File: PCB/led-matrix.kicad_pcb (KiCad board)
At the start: 2 copper layers, 58 x 18 mm, 25 parts, among them J1 Conn_02x03_Odd_Even

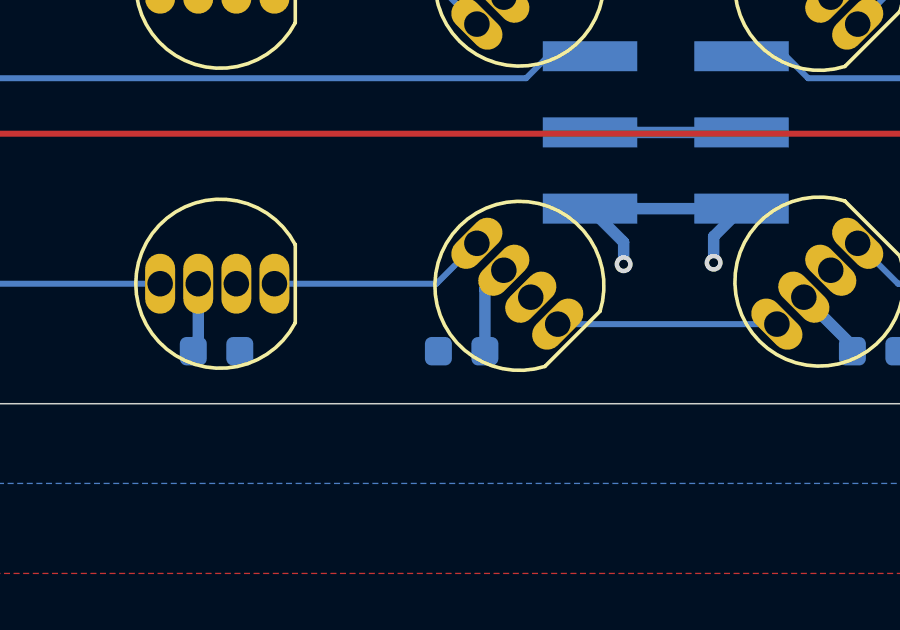
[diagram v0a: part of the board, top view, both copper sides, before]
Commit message: Resolve ground plane island issue
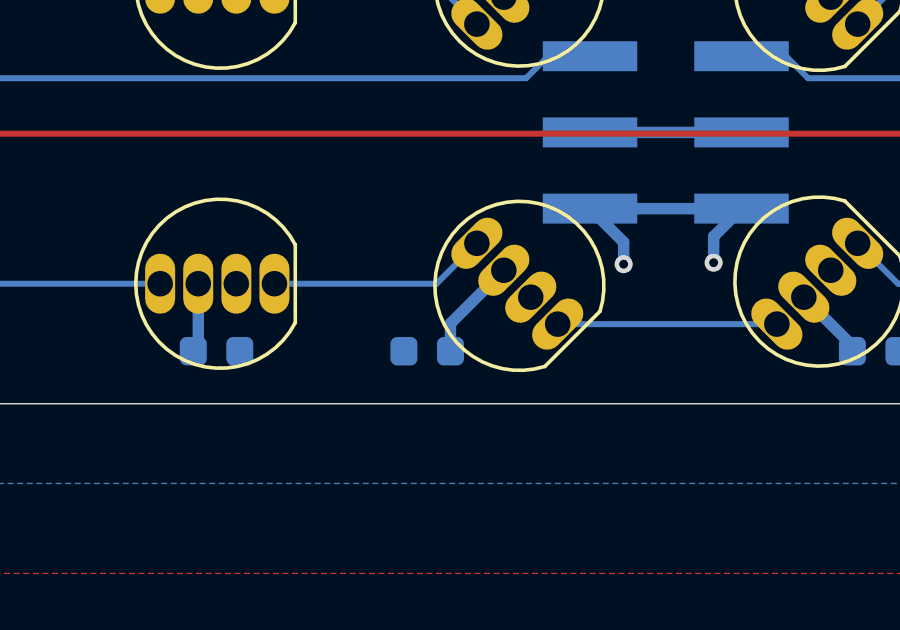
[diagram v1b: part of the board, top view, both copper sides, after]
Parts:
- moved C9 1.15 mm to (95.4, 70.8)
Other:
- board text added: "ImSeanConroy/LED-Matrix (v0.3)"
- board text removed: "ImSeanConroy/LED-Matrix (v0.1)"
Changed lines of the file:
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@@
 	)
 	(paper "A5")
+	(title_block
+		(title "LED Matrix")
+		(date "2025-07-13")
+		(rev "0.3")
+	)
 	(layers
 		(0 "F.Cu" signal)
@@
 			(drillshape 0)
 			(scaleselection 1)
-			(outputdirectory "Fabrication/")
+			(outputdirectory "Fabrication/Gerbers/")
 		)
 	)
@@
 	(footprint "Capacitor_SMD:C_0603_1608Metric"
 		(layer "B.Cu")
-		(at 96.55 70.75 180)
+		(at 95.4024 70.75 180)
 		(descr "Capacitor SMD 0603 (1608 Metric), square (rectangular) end terminal, IPC_7351 nominal, (Body size source: IPC-SM-782 page 76, https://www.pcb-3d.com/wordpress/wp-content/uploads/ipc-sm-782a_amendment_1_and_2.pdf), generated with kicad-footprint-generator")
 		(tags "capacitor")
@@
 		(layer "Edge.Cuts")
 	)
-	(gr_text "ImSeanConroy/LED-Matrix (v0.1)"
+	(gr_text "ImSeanConroy/LED-Matrix (v0.3)"
 		(at 97.8 64.45 0)
 		(layer "B.SilkS")
@@
 	)
 	(segment
-		(start 97.325 68.681974)
-		(end 97.325 70.75)
-		(width 0.381)
-		(layer "B.Cu")
-		(net 1)
-	)
-	(segment
 		(start 107.955987 58.050987)
 		(end 109.5 56.506974)
@@
 	)
 	(segment
+		(start 96.1774 69.829574)
+		(end 96.1774 70.75)
+		(width 0.381)
+		(layer "B.Cu")
+		(net 1)
+	)
+	(segment
 		(start 77.77 70.667189)
 		(end 77.58 70.857189)
@@
 	)
 	(segment
+		(start 97.955987 68.050987)
+		(end 96.1774 69.829574)
+		(width 0.381)
+		(layer "B.Cu")
+		(net 1)
+	)
+	(segment
 		(start 96.325 57.318026)
 		(end 97.955987 58.949013)
@@
 		(width 0.381)
 		(layer "B.Cu")
-		(net 1)
-	)
-	(segment
-		(start 97.955987 68.050987)
-		(end 97.325 68.681974)
-		(width 0.381)
-		(layer "B.Cu")
